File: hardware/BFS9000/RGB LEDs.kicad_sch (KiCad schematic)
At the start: 69 parts, among them J5 Conn_01x01, J6 Conn_01x01

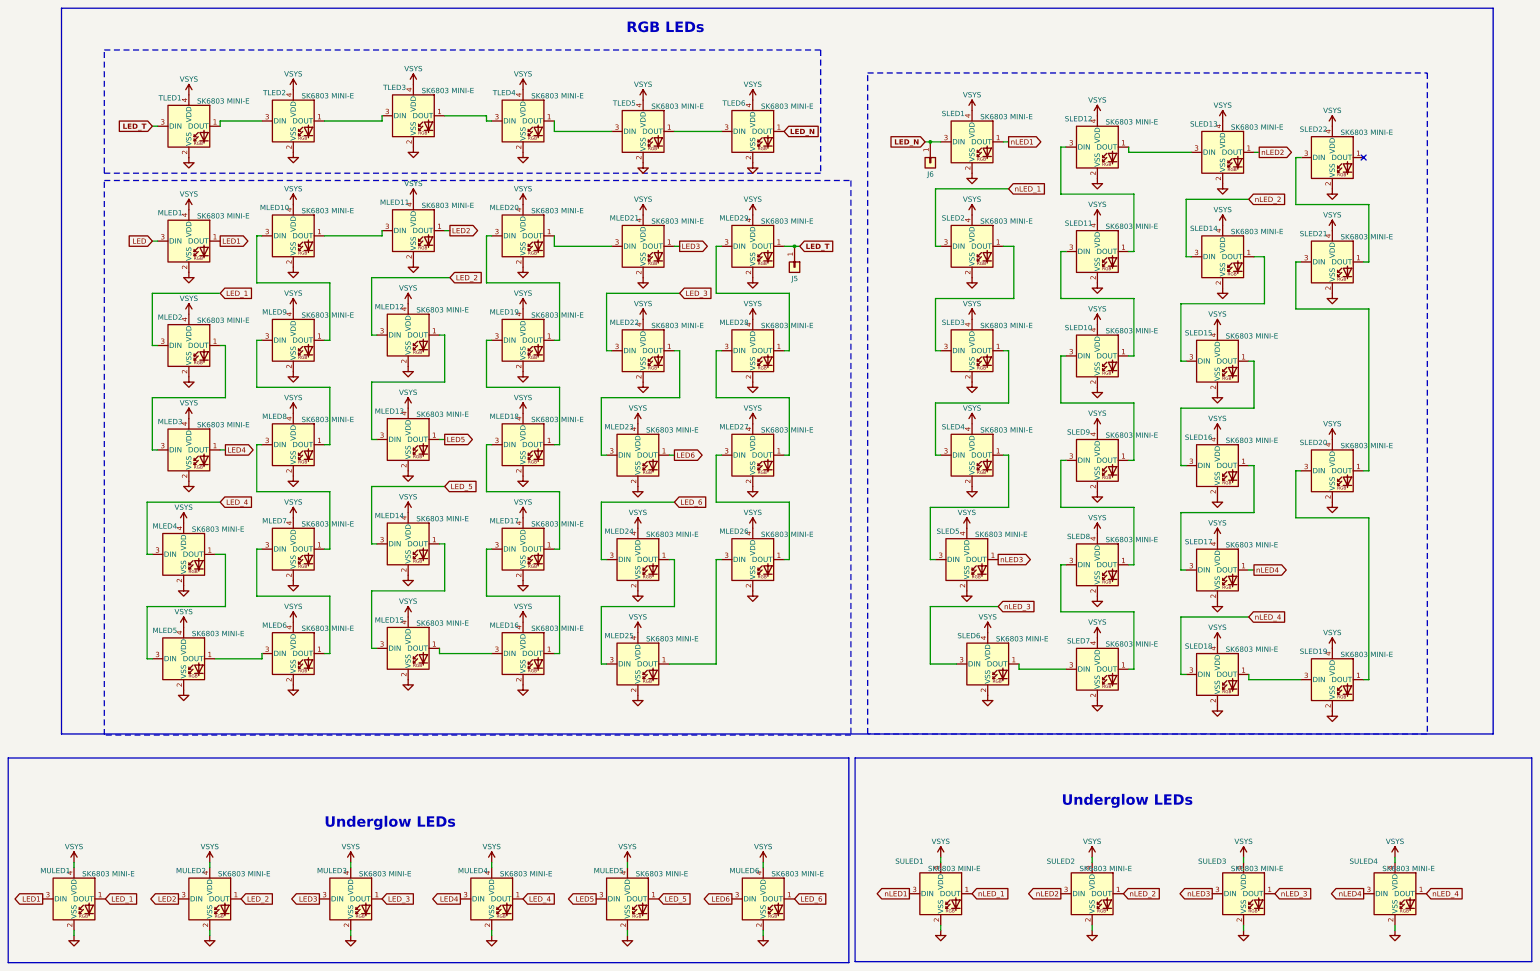
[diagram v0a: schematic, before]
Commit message: feat(hardware): remove MULEDs and reconnect all orphaned traces
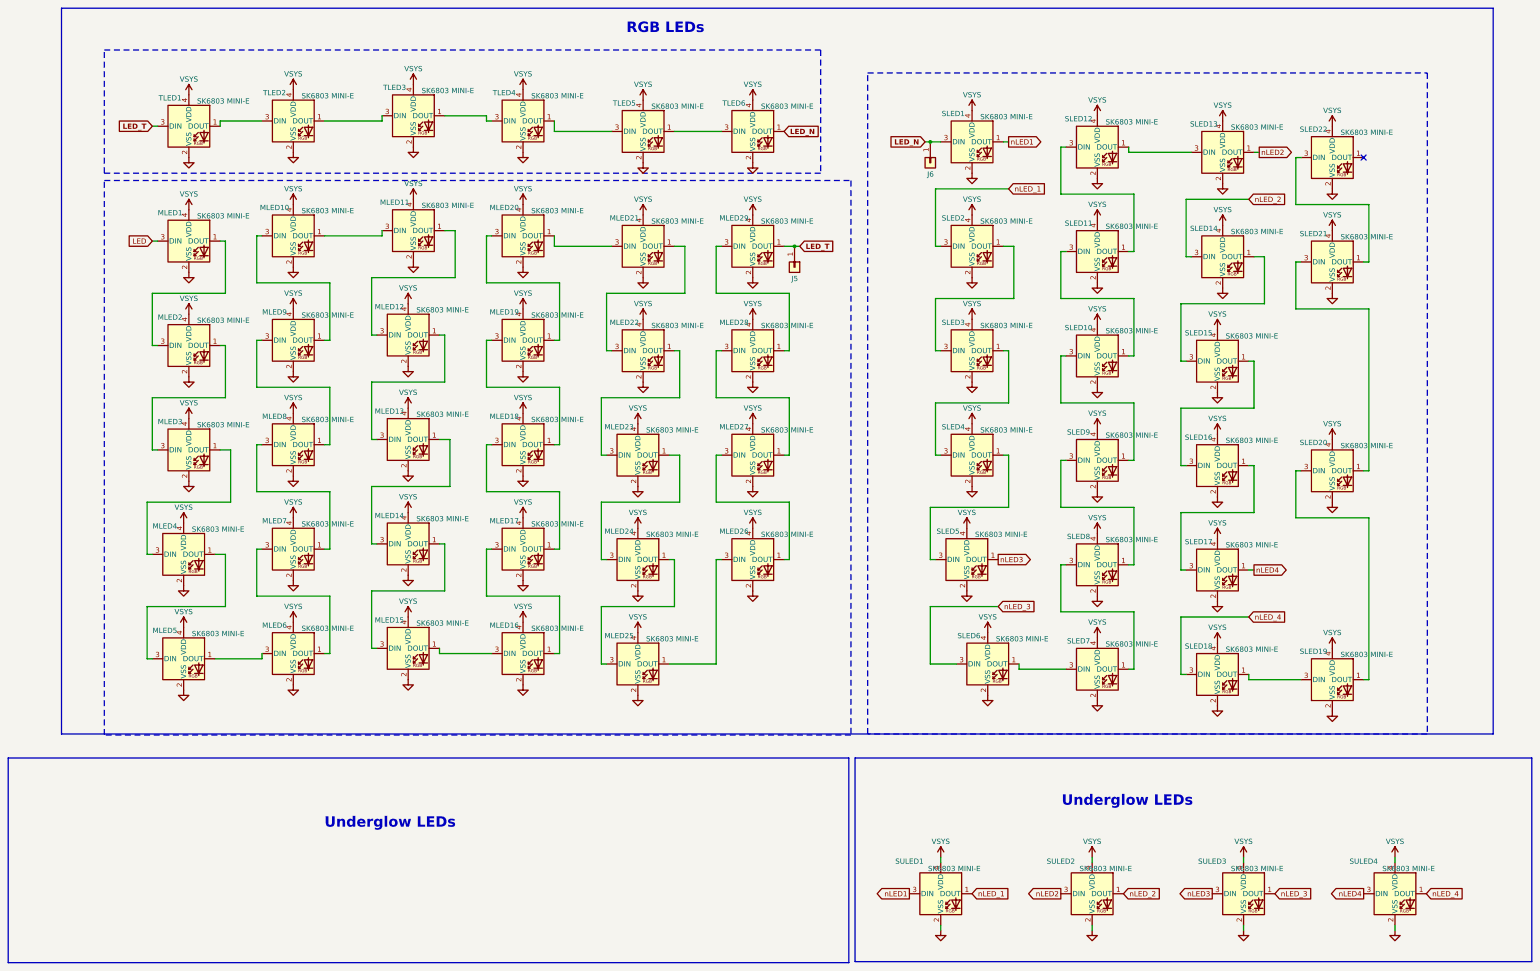
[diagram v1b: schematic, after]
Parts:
- removed MULED1, MULED2, MULED3, MULED4, MULED5, MULED6: SK6803 MINI-E, Sofle_Pico:Cust_SK6803_MINI-E_v3.5.5, symbol LED:SK6805
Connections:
- net LED_1 is gone; now on an unnamed net: MLED2.3 (DIN)
- net LED_2 is gone; now on an unnamed net: MLED12.3 (DIN)
- net LED_3 is gone; now on an unnamed net: MLED22.3 (DIN)
- net LED_4 is gone; now on an unnamed net: MLED4.3 (DIN)
- net LED_5 is gone; now on an unnamed net: MLED14.3 (DIN)
- net LED_6 is gone; now on an unnamed net: MLED24.3 (DIN)
- net LED1: no longer names the net of MLED1.1 (DOUT)
- net LED2: no longer names the net of MLED11.1 (DOUT)
- net LED3: no longer names the net of MLED21.1 (DOUT)
- net LED4: no longer names the net of MLED3.1 (DOUT)
- net LED5: no longer names the net of MLED13.1 (DOUT)
- net LED6: no longer names the net of MLED23.1 (DOUT)
